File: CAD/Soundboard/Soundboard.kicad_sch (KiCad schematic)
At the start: 23 parts, among them P1 USB_C_Plug_USB2.0, SW1 SW_SPST, SW10 SW_SPST, SW11 SW_SPST, SW12 SW_SPST, SW13 SW_SPST, SW14 SW_SPST, SW15 SW_SPST, SW16 SW_SPST, SW2 SW_SPST, SW3 SW_SPST, SW4 SW_SPST, SW5 SW_SPST, SW6 SW_SPST, SW7 SW_SPST, SW8 SW_SPST, SW9 SW_SPST

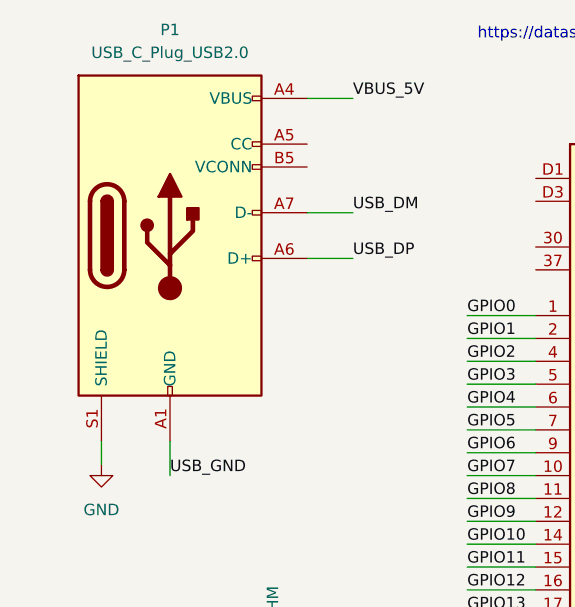
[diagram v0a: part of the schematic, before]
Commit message: add a default layout without routing
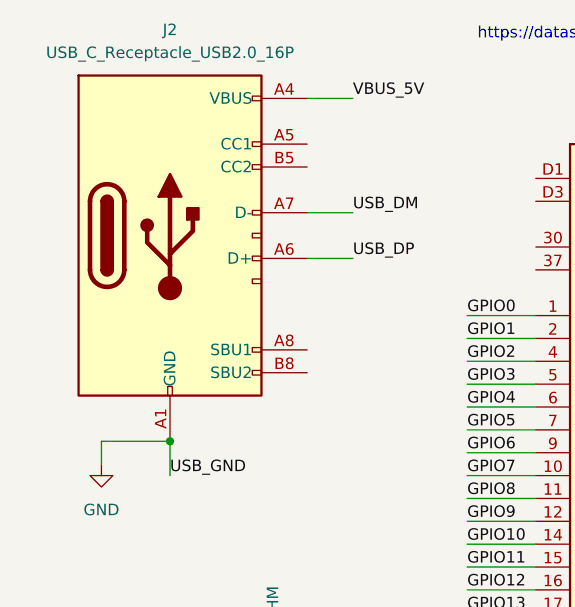
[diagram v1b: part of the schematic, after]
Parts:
- removed P1: USB_C_Plug_USB2.0, symbol Connector:USB_C_Plug_USB2.0
- added J2: USB_C_Receptacle_USB2.0_16P, ubs-c breakout:usb-c breakout, symbol Connector:USB_C_Receptacle_USB2.0_16P
- Brd1: footprint (none) -> Display:Adafruit_SSD1306
- D1, D2: footprint (none) -> LED_THT:LED_D5.0mm_Clear
- R1, R2: footprint (none) -> Resistor_THT:R_Axial_DIN0204_L3.6mm_D1.6mm_P7.62mm_Horizontal
- SW1, SW10, SW11, SW12, SW13, SW14, SW15, SW16, SW2, SW3, SW4, SW5, SW6, SW7, SW8, SW9: footprint (none) -> Switch_Keyboard_Cherry_MX:SW_Cherry_MX_PCB_1.00u
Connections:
- net USB_GND is gone; now on net GND: A1.TP1 (USB_GND)
- net GND: now also J2.A1 (GND), J2.A12 (GND), J2.B1 (GND), J2.B12 (GND)
- net USB_DM: now also J2.A7 (D-)
- net USB_DP: now also J2.A6 (D+)
- net VBUS_5V: now also J2.A4 (VBUS), J2.A9 (VBUS), J2.B4 (VBUS), J2.B9 (VBUS)
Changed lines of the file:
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@@
 	)
 	(junction
+		(at 29.21 60.96)
+		(diameter 0)
+		(color 0 0 0 0)
+	)
+	(junction
 		(at 217.17 48.26)
 		(diameter 0)
@@
 	(wire
 		(pts
+			(xy 21.59 60.96) (xy 29.21 60.96)
+		)
+		(stroke
+			(width 0)
+			(type default)
+		)
+	)
+	(wire
+		(pts
 			(xy 215.9 58.42) (xy 217.17 58.42)
 		)
@@
 			)
 		)
-		(property "Footprint" ""
+		(property "Footprint" "Switch_Keyboard_Cherry_MX:SW_Cherry_MX_PCB_1.00u"
 			(at 187.96 38.1 0)
 			(effects
@@
 			)
 		)
-		(property "Footprint" ""
+		(property "Footprint" "LED_THT:LED_D5.0mm_Clear"
 			(at 29.21 100.33 0)
 			(effects
@@
 			)
 		)
-		(property "Footprint" ""
+		(property "Footprint" "Resistor_THT:R_Axial_DIN0204_L3.6mm_D1.6mm_P7.62mm_Horizontal"
 			(at 39.37 102.108 90)
 			(effects
@@
 			)
 		)
-		(property "Footprint" ""
+		(property "Footprint" "Switch_Keyboard_Cherry_MX:SW_Cherry_MX_PCB_1.00u"
 			(at 187.96 27.94 0)
 			(effects
@@
 			)
 		)
-		(property "Footprint" ""
+		(property "Footprint" "Switch_Keyboard_Cherry_MX:SW_Cherry_MX_PCB_1.00u"
 			(at 166.37 38.1 0)
 			(effects
@@
 			)
 		)
-		(property "Footprint" ""
+		(property "Footprint" "Display:Adafruit_SSD1306"
 			(at 29.21 124.46 0)
 			(effects
@@
 			)
 		)
-		(property "Footprint" ""
+		(property "Footprint" "Switch_Keyboard_Cherry_MX:SW_Cherry_MX_PCB_1.00u"
 			(at 210.82 27.94 0)
 			(effects
@@
 			)
 		)
-		(property "Footprint" ""
+		(property "Footprint" "Switch_Keyboard_Cherry_MX:SW_Cherry_MX_PCB_1.00u"
 			(at 210.82 48.26 0)
 			(effects
@@
 			)
 		)
-		(property "Footprint" ""
+		(property "Footprint" "Switch_Keyboard_Cherry_MX:SW_Cherry_MX_PCB_1.00u"
 			(at 143.51 38.1 0)
 			(effects
@@
 	)
 	(symbol
+		(lib_name "USB_C_Receptacle_USB2.0_16P_1")
+		(lib_id "Connector:USB_C_Receptacle_USB2.0_16P")
+		(at 29.21 38.1 0)
+		(unit 1)
+		(exclude_from_sim no)
+		(in_bom yes)
+		(on_board yes)
+		(dnp no)
+		(fields_autoplaced yes)
+		(property "Reference" "J2"
+			(at 29.21 15.24 0)
+			(effects
+				(font
+					(size 1.27 1.27)
+				)
+			)
+		)
+		(property "Value" "USB_C_Receptacle_USB2.0_16P"
+			(at 29.21 17.78 0)
+			(effects
+				(font
+					(size 1.27 1.27)
+				)
+			)
+		)
+		(property "Footprint" "ubs-c breakout:usb-c breakout"
+			(at 33.02 38.1 0)
+			(effects
+				(font
+					(size 1.27 1.27)
+				)
+				(hide yes)
+			)
+		)
+		(property "Datasheet" "https://www.usb.org/sites/default/files/documents/usb_type-c.zip"
+			(at 33.02 38.1 0)
+			(effects
+				(font
+					(size 1.27 1.27)
+				)
+				(hide yes)
+			)
+		)
+		(property "Description" "USB 2.0-only 16P Type-C Receptacle connector"
+			(at 29.21 38.1 0)
+			(effects
+				(font
+					(size 1.27 1.27)
+				)
+				(hide yes)
+			)
+		)
+		(pin "A4"
+		)
+		(pin "A1"
+		)
+		(pin "A12"
+		)
+		(pin "B1"
+		)
+		(pin "B12"
+		)
+		(pin "B4"
+		)
+		(pin "B9"
+		)
+		(pin "A5"
+		)
+		(pin "A9"
+		)
+		(pin "A7"
+		)
+		(pin "A6"
+		)
+		(pin "B8"
+		)
+		(pin "A8"
+		)
+		(pin "B5"
+		)
+		(instances
+			(project ""
+				(path "/d37aae72-d95c-45f1-8f5f-848ee8bbabd0"
+					(reference "J2")
+					(unit 1)
+				)
+			)
+		)
+	)
+	(symbol
 		(lib_id "power:GND")
 		(at 19.05 101.6 0)
@@
 			)
 		)
-		(property "Footprint" ""
+		(property "Footprint" "Switch_Keyboard_Cherry_MX:SW_Cherry_MX_PCB_1.00u"
 			(at 210.82 58.42 0)
 			(effects
@@
 			)
 		)
-		(property "Footprint" ""
+		(property "Footprint" "Switch_Keyboard_Cherry_MX:SW_Cherry_MX_PCB_1.00u"
 			(at 166.37 27.94 0)
 			(effects
@@
 			)
 		)
-		(property "Footprint" ""
+		(property "Footprint" "Switch_Keyboard_Cherry_MX:SW_Cherry_MX_PCB_1.00u"
 			(at 166.37 48.26 0)
 			(effects
@@
 			)
 		)
-		(property "Footprint" ""
+		(property "Footprint" "Switch_Keyboard_Cherry_MX:SW_Cherry_MX_PCB_1.00u"
 			(at 187.96 58.42 0)
 			(effects
@@
 			)
 		)
-		(property "Footprint" ""
+		(property "Footprint" "Switch_Keyboard_Cherry_MX:SW_Cherry_MX_PCB_1.00u"
 			(at 143.51 48.26 0)
 			(effects
@@
 			)
 		)
-		(property "Footprint" ""
+		(property "Footprint" "Switch_Keyboard_Cherry_MX:SW_Cherry_MX_PCB_1.00u"
 			(at 166.37 58.42 0)
 			(effects
@@
 			)
 		)
-		(property "Footprint" ""
+		(property "Footprint" "Switch_Keyboard_Cherry_MX:SW_Cherry_MX_PCB_1.00u"
 			(at 210.82 38.1 0)
 			(effects
@@
 	)
 	(symbol
-		(lib_id "Connector:USB_C_Plug_USB2.0")
-		(at 29.21 38.1 0)
-		(unit 1)
-		(exclude_from_sim no)
-		(in_bom yes)
-		(on_board yes)
-		(dnp no)
-		(fields_autoplaced yes)
-		(property "Reference" "P1"
-			(at 29.21 15.24 0)
-			(effects
-				(font
-					(size 1.27 1.27)
-				)
-			)
-		)
-		(property "Value" "USB_C_Plug_USB2.0"
-			(at 29.21 17.78 0)
-			(effects
-				(font
-					(size 1.27 1.27)
-				)
-			)
-		)
-		(property "Footprint" ""
-			(at 33.02 38.1 0)
-			(effects
-				(font
-					(size 1.27 1.27)
-				)
-				(hide yes)
-			)
-		)
-		(property "Datasheet" "https://www.usb.org/sites/default/files/documents/usb_type-c.zip"
-			(at 33.02 38.1 0)
-			(effects
-				(font
-					(size 1.27 1.27)
-				)
-				(hide yes)
-			)
-		)
-		(property "Description" "USB 2.0-only Type-C Plug connector"
-			(at 29.21 38.1 0)
-			(effects
-				(font
-					(size 1.27 1.27)
-				)
-				(hide yes)
-			)
-		)
-		(pin "B4"
-		)
-		(pin "A9"
-		)
-		(pin "A4"
-		)
-		(pin "B9"
-		)
-		(pin "A5"
-		)
-		(pin "B5"
-		)
-		(pin "A7"
-		)
-		(pin "A6"
-		)
-		(pin "A1"
-		)
-		(pin "A12"
-		)
-		(pin "B1"
-		)
-		(pin "B12"
-		)
-		(pin "S1"
-		)
-		(instances
-			(project ""
-				(path "/d37aae72-d95c-45f1-8f5f-848ee8bbabd0"
-					(reference "P1")
-					(unit 1)
-				)
-			)
-		)
-	)
-	(symbol
 		(lib_id "Switch:SW_SPST")
 		(at 143.51 58.42 0)
@@
 			)
 		)
-		(property "Footprint" ""
+		(property "Footprint" "Switch_Keyboard_Cherry_MX:SW_Cherry_MX_PCB_1.00u"
 			(at 143.51 58.42 0)
 			(effects
@@
 			)
 		)
-		(property "Footprint" ""
+		(property "Footprint" "LED_THT:LED_D5.0mm_Clear"
 			(at 29.21 87.63 0)
 			(effects
@@
 			)
 		)
-		(property "Footprint" ""
+		(property "Footprint" "Switch_Keyboard_Cherry_MX:SW_Cherry_MX_PCB_1.00u"
 			(at 187.96 48.26 0)
 			(effects
@@
 			)
 		)
-		(property "Footprint" ""
+		(property "Footprint" "Switch_Keyboard_Cherry_MX:SW_Cherry_MX_PCB_1.00u"
 			(at 143.51 27.94 0)
 			(effects
@@
 			)
 		)
-		(property "Footprint" ""
+		(property "Footprint" "Resistor_THT:R_Axial_DIN0204_L3.6mm_D1.6mm_P7.62mm_Horizontal"
 			(at 39.37 89.408 90)
 			(effects

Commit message: big changes boys
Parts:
- removed J2: USB_C_Receptacle_USB2.0_16P, ubs-c breakout:usb-c breakout, symbol Connector:USB_C_Receptacle_USB2.0_16P
- added C1: I dont know something big, Capacitor_SMD:C_0805_2012Metric, symbol Device:C
- added D10, D11, D12, D13, D14, D15, D16, D17, D18, D3, D4, D5, D6, D7, D8, D9: ASMB-MTB1-0A3A2, LED_SMD:LED_Avago_PLCC4_3.2x2.8mm_CW, symbol LED:ASMB-MTB1-0A3A2
- added J1: USB4085-GF-A_REVB, USB4085-GF-A_REVB:GCT_USB4085-GF-A_REVB, symbol USB4085-GF-A_REVB:USB4085-GF-A_REVB
- added JP1: HEADER-1X876MIL, Connector_PinHeader_2.54mm:PinHeader_1x08_P2.54mm_Vertical, symbol Adafruit USB Type C Downstream Breakout rev B-eagle-import:HEADER-1X876MIL
- added Q1, Q2, Q3, Q4: IRLML6401, Package_TO_SOT_SMD:SOT-23, symbol Transistor_FET:IRLML6401
- added R3, R4: 5.1K, Resistor_SMD:R_0805_2012Metric, symbol Adafruit USB Type C Downstream Breakout rev B-eagle-import:RESISTOR_0603_NOOUT
- added R5, R6, R7, R8: 300, Resistor_SMD:R_0805_2012Metric, symbol Device:R
- added R9: 2.2 K, Resistor_SMD:R_0805_2012Metric, symbol Device:R
- added U1: TLC59283DBQ, TLC59283DBQ:DBQ24_TEX, symbol TLC59283DBQ:TLC59283DBQ
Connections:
- net GND: now also C1.1, J1.A1 (GND), J1.A12 (GND), J1.B1 (GND), J1.B12 (GND), J1.S1 (SHELL), J1.S2 (SHELL), J1.S3 (SHELL), J1.S4 (SHELL), JP1.1, R3.1, R4.1, R9.1, U1.1 (GND)
- net GPIO22: now also A1.29 (GPIO22)
- net GPIO28: now also A1.34 (GPIO28_ADC2)
- net LED LAT: now reaches A1.21 (GPIO16)
- net LED LAT: now also U1.4 (LAT)
- net LED BLANK: now reaches A1.22 (GPIO17)
- net LED BLANK: now also U1.21 (BLANK)
- net LED SIN: now reaches A1.24 (GPIO18)
- net LED SIN: now also U1.2 (SIN)
- net LED SCLK: now reaches A1.25 (GPIO19)
- net LED SCLK: now also U1.3 (SCLK)
- net VBUS: now reaches A1.39 (VSYS)
- net VBUS: now also J1.A4 (VBUS), J1.A9 (VBUS), J1.B4 (VBUS), J1.B9 (VBUS), JP1.2
- net USB_DM renamed D-
- net D-: now also J1.A7 (DN1), J1.B7 (DN2), JP1.5
- net USB_DP renamed D+
- net D+: now also J1.A6 (DP1), J1.B6 (DP2), JP1.6
- net VBUS_5V: no longer names the net of A1.40 (VBUS)
- new net: D11.1 (RK), D15.1 (RK), D3.1 (RK), D7.1 (RK), U1.20 (OUT15)
- new net: D11.2 (GK), D15.2 (GK), D3.2 (GK), D7.2 (GK), U1.19 (OUT14)
- new net: D11.3 (BK), D15.3 (BK), D3.3 (BK), D7.3 (BK), U1.18 (OUT13)
- new net: D10.4 (A), D7.4 (A), D8.4 (A), D9.4 (A), Q4.3 (D)
- new net: Q2.1 (G), R6.2, U1.6 (OUT1)
- new net: Q1.2 (S), Q2.2 (S), Q3.2 (S), Q4.2 (S), R5.1, R6.1, R7.1, R8.1
- new net: D11.4 (A), D12.4 (A), D13.4 (A), D14.4 (A), Q2.3 (D)
- new net: D13.1 (RK), D17.1 (RK), D5.1 (RK), D9.1 (RK), U1.14 (OUT9)
- new net: D13.2 (GK), D17.2 (GK), D5.2 (GK), D9.2 (GK), U1.13 (OUT8)
- new net: D13.3 (BK), D17.3 (BK), D5.3 (BK), D9.3 (BK), U1.12 (OUT7)
- new net: D3.4 (A), D4.4 (A), D5.4 (A), D6.4 (A), Q3.3 (D)
- new net: C1.2, U1.24 (VCC)
- new net: D10.1 (RK), D14.1 (RK), D18.1 (RK), D6.1 (RK), U1.11 (OUT6)
- new net: D10.2 (GK), D14.2 (GK), D18.2 (GK), D6.2 (GK), U1.10 (OUT5)
- new net: D10.3 (BK), D14.3 (BK), D18.3 (BK), D6.3 (BK), U1.9 (OUT4)
- new net: Q3.1 (G), R7.2, U1.7 (OUT2)
- new net: R9.2, U1.23 (IREF)
- new net: D12.1 (RK), D16.1 (RK), D4.1 (RK), D8.1 (RK), U1.17 (OUT12)
- new net: D12.2 (GK), D16.2 (GK), D4.2 (GK), D8.2 (GK), U1.16 (OUT11)
- new net: D12.3 (BK), D16.3 (BK), D4.3 (BK), D8.3 (BK), U1.15 (OUT10)
- new net: Q1.1 (G), R5.2, U1.5 (OUT0)
- new net: Q4.1 (G), R8.2, U1.8 (OUT3)
- new net: D15.4 (A), D16.4 (A), D17.4 (A), D18.4 (A), Q1.3 (D)
- new net CC1: J1.B5 (CC2), JP1.4, R4.2
- new net CC2: J1.A5 (CC1), JP1.8, R3.2
- new net SBU1: J1.A8 (SBU1), JP1.7
- new net SBU2: J1.B8 (SBU2), JP1.3
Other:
- note added: "Please note, the TLC59283DBQ's referance current should be set to aprox. 25mA with a 2.2K resistor with 25mA the P channel transistor the minimium value of the pull up resitor is given by r_min = enabled_voltage / sink_current from this we get the min R is 180 Some testing may review a better higher value. I think we will start with 300"
- note added: "Set to UFP (Peripheral) Also marks this as a USB 2.0 peripheral device For DFP (Host) you need pullups here instead of pulldowns."
- note added: "Upstream/Downstream Facing Port Setup:"
- moved on the sheet: Brd1, D1, D2, R1, R2

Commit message: do all the things
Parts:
- renumbered D15 to ST1, D13 to ST10, D5 to ST11, D9 to ST12, D18 to ST13, D14 to ST14, D6 to ST15, D10 to ST16, D11 to ST2, D3 to ST3, D7 to ST4, D16 to ST5, D12 to ST6, D4 to ST7, D8 to ST8, D17 to ST9
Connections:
- net GPIO0: now also SW4.1 (A); no longer SW1.1 (A)
- net GPIO1: now also SW3.1 (A); no longer SW2.1 (A)
- net GPIO10: now also SW10.1 (A); no longer SW11.1 (A)
- net GPIO11: now also SW9.1 (A); no longer SW12.1 (A)
- net GPIO12: now also SW16.1 (A); no longer SW13.1 (A)
- net GPIO13: now also SW15.1 (A); no longer SW14.1 (A)
- net GPIO14: now also SW14.1 (A); no longer SW15.1 (A)
- net GPIO15: now also SW13.1 (A); no longer SW16.1 (A)
- net GPIO2: now also SW2.1 (A); no longer SW3.1 (A)
- net GPIO3: now also SW1.1 (A); no longer SW4.1 (A)
- net GPIO4: now also SW8.1 (A); no longer SW5.1 (A)
- net GPIO5: now also SW7.1 (A); no longer SW6.1 (A)
- net GPIO6: now also SW6.1 (A); no longer SW7.1 (A)
- net GPIO7: now also SW5.1 (A); no longer SW8.1 (A)
- net GPIO8: now also SW12.1 (A); no longer SW9.1 (A)
- net GPIO9: now also SW11.1 (A); no longer SW10.1 (A)
- net at ST1.1 (RK), ST2.1 (RK), ST3.1 (RK)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: now also U1.9 (OUT4); no longer U1.20 (OUT15)
- net at ST1.2 (GK), ST2.2 (GK), ST3.2 (GK)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: now also U1.10 (OUT5); no longer U1.19 (OUT14)
- net at ST1.3 (BK), ST2.3 (BK), ST3.3 (BK)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: now also U1.11 (OUT6); no longer U1.18 (OUT13)
- net at ST10.1 (RK), ST11.1 (RK), ST12.1 (RK)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: now also U1.15 (OUT10); no longer U1.14 (OUT9)
- net at ST10.2 (GK), ST11.2 (GK), ST12.2 (GK)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: now also U1.16 (OUT11); no longer U1.13 (OUT8)
- net at ST10.3 (BK), ST11.3 (BK), ST12.3 (BK)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: now also U1.17 (OUT12); no longer U1.12 (OUT7)
- net at ST13.1 (RK), ST14.1 (RK), ST15.1 (RK)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: now also U1.18 (OUT13); no longer U1.11 (OUT6)
- net at ST13.2 (GK), ST14.2 (GK), ST15.2 (GK)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: now also U1.19 (OUT14); no longer U1.10 (OUT5)
- net at ST13.3 (BK), ST14.3 (BK), ST15.3 (BK)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: now also U1.20 (OUT15); no longer U1.9 (OUT4)
- net at ST5.1 (RK), ST6.1 (RK), ST7.1 (RK)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: now also U1.12 (OUT7); no longer U1.17 (OUT12)
- net at ST5.2 (GK), ST6.2 (GK), ST7.2 (GK)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: now also U1.13 (OUT8); no longer U1.16 (OUT11)
- net at ST5.3 (BK), ST6.3 (BK), ST7.3 (BK)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: now also U1.14 (OUT9); no longer U1.15 (OUT10)
